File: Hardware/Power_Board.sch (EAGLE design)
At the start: 38 parts, among them K1 E3206S, K2 E3206S, K3 E3206S, K4 E3206S, K5 E3206S, K6 E3206S, Q1 BD135, Q2 BD135, Q3 BD135, Q4 BD135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

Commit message: Updated schematic files to Eagle 8.3.1 and added the AC/DC converter to the power board.
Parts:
- added U$1: VTX-214-010-205, VTX-214-010-205:VTX-214-010-205
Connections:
- net GND: now also U$1.GND
- net N$10: now also U$1.LIVE
- net N$31: now also U$1.NEUTRAL
- net VCC: now also U$1.+5V
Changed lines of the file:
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@@
 <?xml version="1.0" encoding="utf-8"?>
 <!DOCTYPE eagle SYSTEM "eagle.dtd">
-<eagle version="7.5.0">
+<eagle version="8.3.1">
 <drawing>
 <settings>
 <setting alwaysvectorfont="no"/>
+<setting keepoldvectorfont="yes"/>
 <setting verticaltext="down"/>
 </settings>
-<grid distance="0.1" unitdist="inch" unit="inch" style="lines" multiple="1" display="yes" altdistance="0.01" altunitdist="inch" altunit="inch"/>
+<grid distance="0.1" unitdist="inch" unit="inch" style="dots" multiple="1" display="yes" altdistance="0.01" altunitdist="inch" altunit="inch"/>
 <layers>
 <layer number="1" name="Top" color="4" fill="1" visible="no" active="no"/>
@@
 <part name="R5" library="resistor" deviceset="R-EU_" device="0207/10" value="1K"/>
 <part name="R6" library="resistor" deviceset="R-EU_" device="0207/10" value="1K"/>
+<part name="U$1" library="VTX-214-010-205" deviceset="VTX-214-010-205" device=""/>
+<part name="GND4" library="supply1" deviceset="GND" device=""/>
+<part name="P+1" library="supply1" deviceset="VCC" device=""/>
 </parts>
 <sheets>
@@
 <instance part="R5" gate="G$1" x="297.18" y="195.58"/>
 <instance part="R6" gate="G$1" x="297.18" y="165.1"/>
+<instance part="U$1" gate="G$1" x="35.56" y="332.74"/>
+<instance part="GND4" gate="1" x="73.66" y="327.66"/>
+<instance part="P+1" gate="VCC" x="76.2" y="342.9" rot="R270"/>
 </instances>
 <busses>
@@
 <pinref part="GND1" gate="1" pin="GND"/>
 <wire x1="109.22" y1="142.24" x2="109.22" y2="149.86" width="0.1524" layer="91"/>
+</segment>
+<segment>
+<pinref part="U$1" gate="G$1" pin="GND"/>
+<wire x1="68.58" y1="332.74" x2="73.66" y2="332.74" width="0.1524" layer="91"/>
+<pinref part="GND4" gate="1" pin="GND"/>
+<wire x1="73.66" y1="332.74" x2="73.66" y2="330.2" width="0.1524" layer="91"/>
 </segment>
 </net>
@@
 <pinref part="P+4" gate="VCC" pin="VCC"/>
 <wire x1="116.84" y1="144.78" x2="116.84" y2="149.86" width="0.1524" layer="91"/>
+</segment>
+<segment>
+<pinref part="U$1" gate="G$1" pin="+5V"/>
+<pinref part="P+1" gate="VCC" pin="VCC"/>
+<wire x1="68.58" y1="342.9" x2="73.66" y2="342.9" width="0.1524" layer="91"/>
 </segment>
 </net>
@@
 <wire x1="-5.08" y1="243.84" x2="-53.34" y2="243.84" width="0.1524" layer="91"/>
 <junction x="-53.34" y="243.84"/>
-<wire x1="-35.56" y1="304.8" x2="195.58" y2="304.8" width="0.1524" layer="91"/>
+<wire x1="-35.56" y1="304.8" x2="-5.08" y2="304.8" width="0.1524" layer="91"/>
+<wire x1="-5.08" y1="304.8" x2="195.58" y2="304.8" width="0.1524" layer="91"/>
 <wire x1="195.58" y1="304.8" x2="195.58" y2="243.84" width="0.1524" layer="91"/>
 <junction x="-35.56" y="304.8"/>
@@
 <wire x1="213.36" y1="187.96" x2="213.36" y2="182.88" width="0.1524" layer="91"/>
 <wire x1="213.36" y1="182.88" x2="195.58" y2="182.88" width="0.1524" layer="91"/>
+<wire x1="-5.08" y1="304.8" x2="-5.08" y2="322.58" width="0.1524" layer="91"/>
+<pinref part="U$1" gate="G$1" pin="LIVE"/>
+<wire x1="-5.08" y1="322.58" x2="2.54" y2="322.58" width="0.1524" layer="91"/>
+<junction x="-5.08" y="304.8"/>
 </segment>
 </net>
@@
 <wire x1="-35.56" y1="279.4" x2="-40.64" y2="279.4" width="0.1524" layer="91"/>
 <wire x1="-35.56" y1="287.02" x2="-35.56" y2="279.4" width="0.1524" layer="91"/>
-<wire x1="-35.56" y1="287.02" x2="190.5" y2="287.02" width="0.1524" layer="91"/>
+<wire x1="-35.56" y1="287.02" x2="-10.16" y2="287.02" width="0.1524" layer="91"/>
 <junction x="-35.56" y="287.02"/>
+<wire x1="-10.16" y1="287.02" x2="190.5" y2="287.02" width="0.1524" layer="91"/>
 <wire x1="-35.56" y1="294.64" x2="-35.56" y2="287.02" width="0.1524" layer="91"/>
 <pinref part="PAD11" gate="G$1" pin="P"/>
@@
 <wire x1="213.36" y1="213.36" x2="190.5" y2="213.36" width="0.1524" layer="91"/>
 <junction x="190.5" y="213.36"/>
+<wire x1="-10.16" y1="287.02" x2="-10.16" y2="342.9" width="0.1524" layer="91"/>
+<pinref part="U$1" gate="G$1" pin="NEUTRAL"/>
+<wire x1="-10.16" y1="342.9" x2="2.54" y2="342.9" width="0.1524" layer="91"/>
+<junction x="-10.16" y="287.02"/>
 </segment>
 </net>
@@
 </sheet>
 </sheets>
+<errors>
+</errors>
 </schematic>
 </drawing>

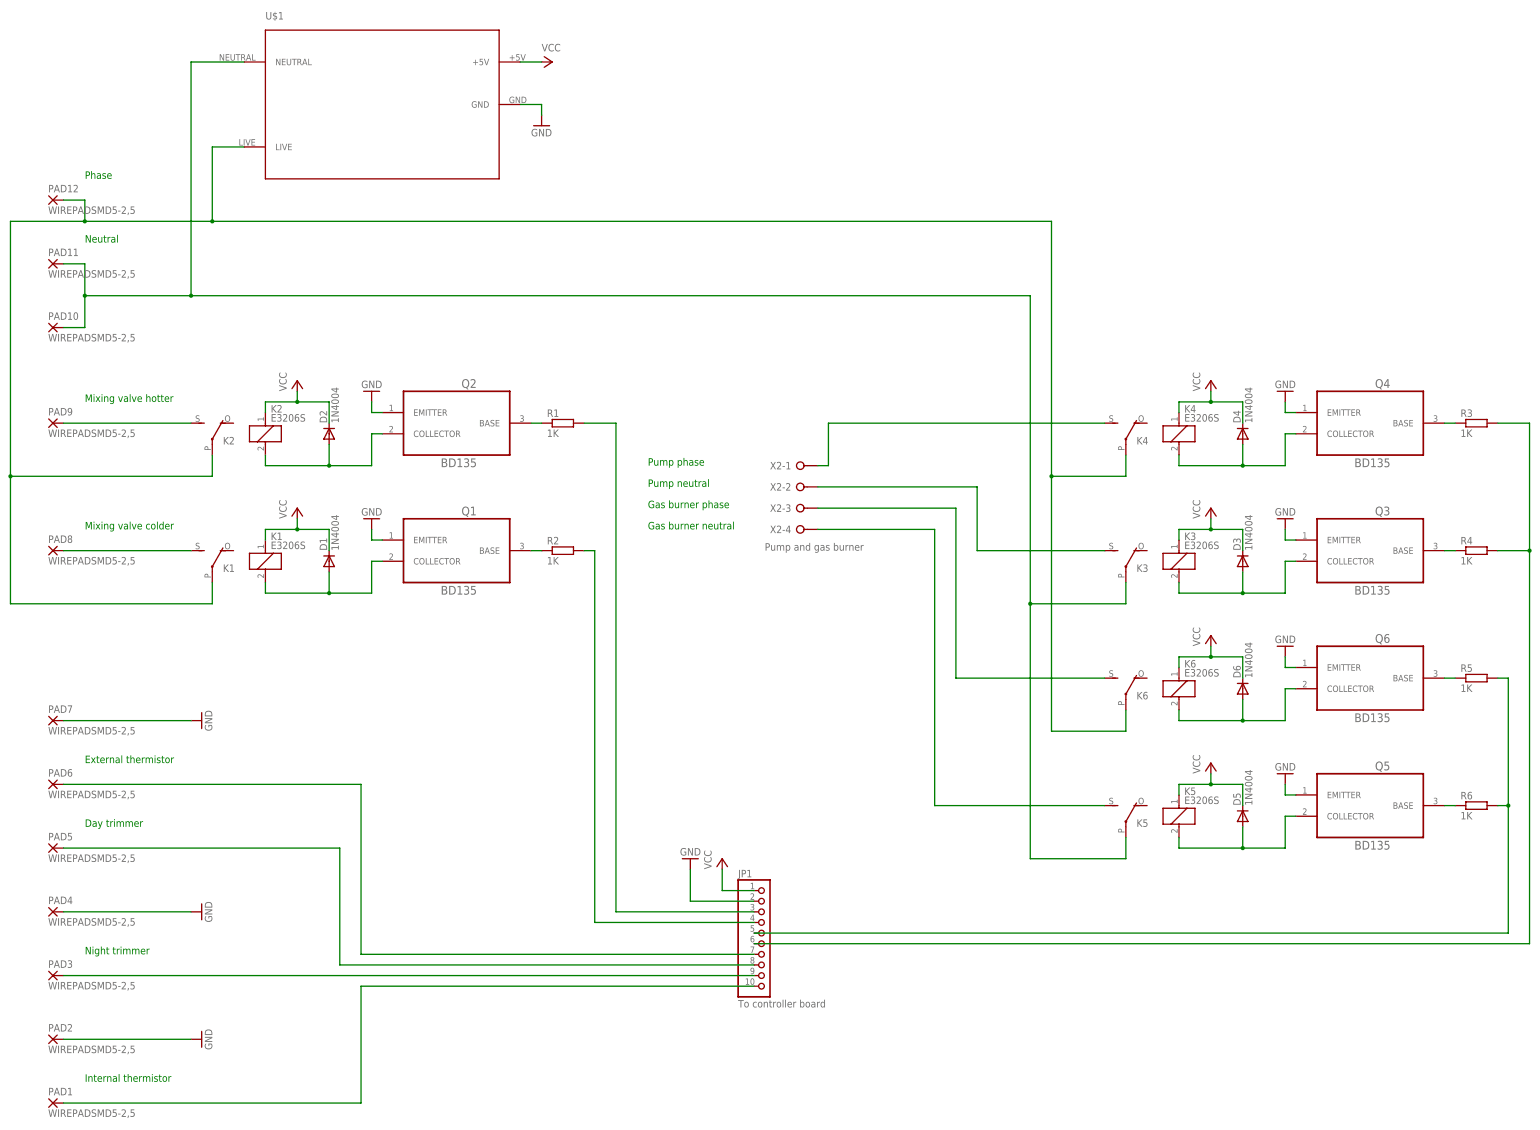
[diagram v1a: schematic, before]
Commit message: Added a 2-pad terminal to supply the pump and the gas burner from a different 230V source than the one provided by the wall housing, which might not be powerful enough.
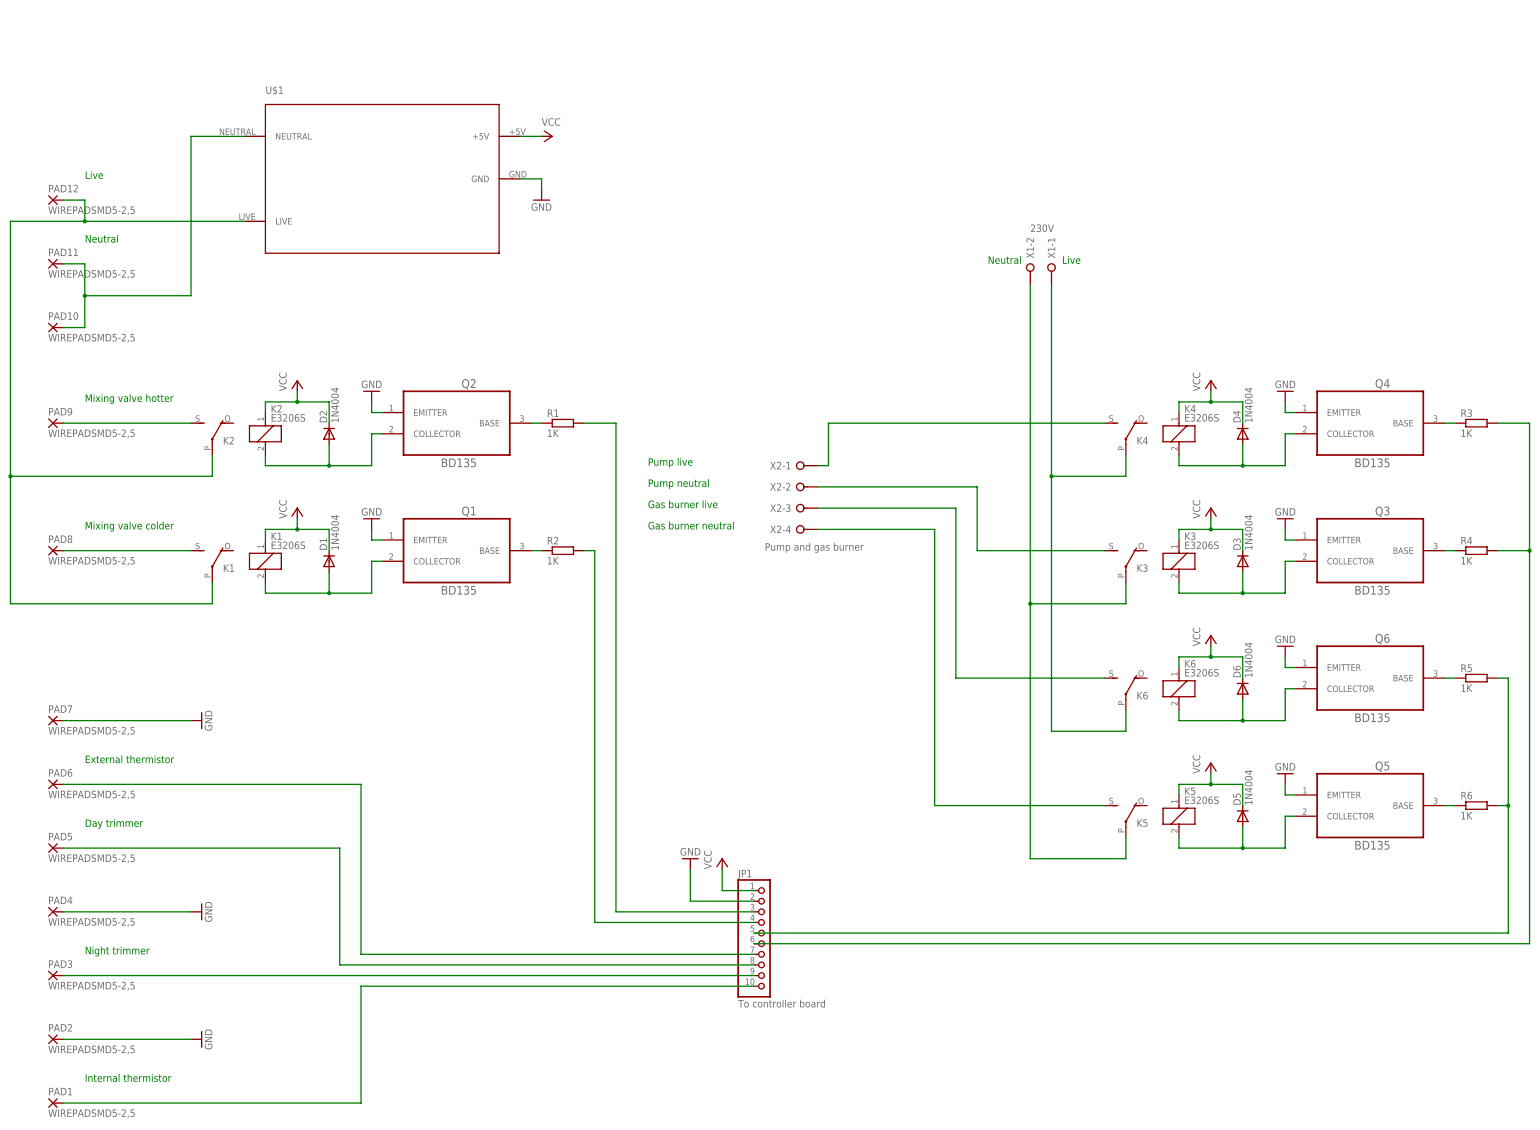
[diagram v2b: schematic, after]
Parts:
- added X1: 230V, con-wago-508:W237-02P
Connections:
- removed net N$31: K32.P, K52.P, PAD10.P, PAD11.P, U$1.NEUTRAL
- new net N$25: K42.P, K62.P, X1-1.KL
- new net N$27: PAD10.P, PAD11.P, U$1.NEUTRAL
- new net N$28: K32.P, K52.P, X1-2.KL
- net N$10: no longer K42.P, K62.P
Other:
- note added: "Gas burner live"
- note added: "Live"
- note added: "Pump live"
- note removed: "Gas burner phase"
- note removed: "Phase"
- note removed: "Pump phase"
- moved on the sheet: U$1
